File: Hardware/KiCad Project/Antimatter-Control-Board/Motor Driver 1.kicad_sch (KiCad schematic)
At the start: 3 parts, among them J2 MOTOR 1, U3 DRV8837

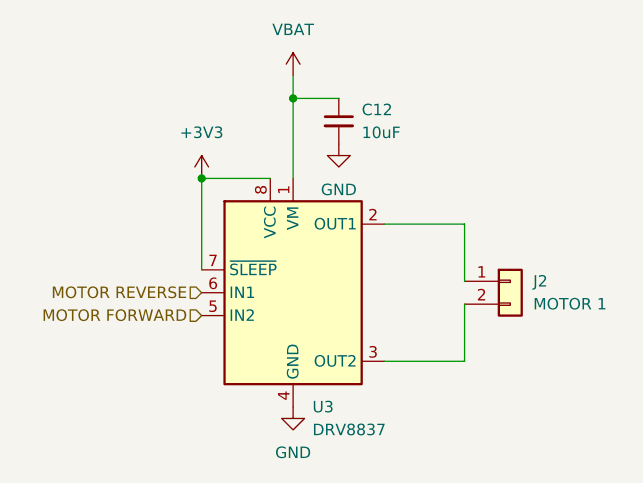
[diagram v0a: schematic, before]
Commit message: Update motor driver sheet
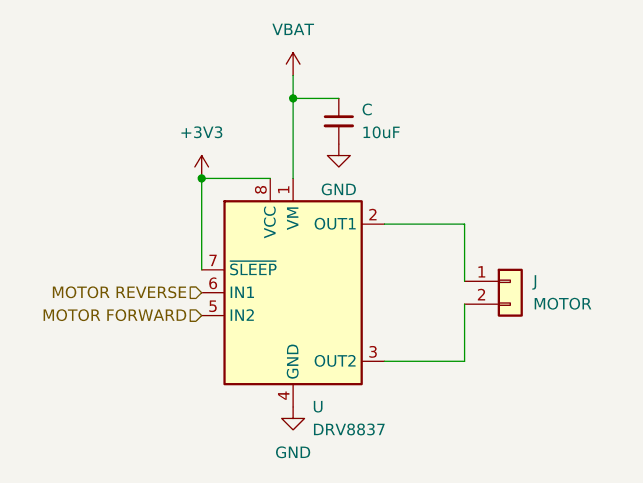
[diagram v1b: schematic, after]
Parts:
- J: renamed from J2; value MOTOR 1 -> MOTOR
- renumbered C12 to C, U3 to U
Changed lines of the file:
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@@
 		(dnp no)
 		(fields_autoplaced yes)
-		(property "Reference" "#PWR021"
+		(property "Reference" "#PWR"
 			(at 138.43 88.9 0)
 			(effects
@@
 		)
 		(instances
-			(project ""
-				(path "/ab2a7697-0e5e-4b53-bb59-6796636b3acd/d7ef5df8-638b-454c-90c6-da1c11f20dab"
-					(reference "#PWR021")
+			(project "Antimatter-Control-Board"
+				(path "/ab2a7697-0e5e-4b53-bb59-6796636b3acd/bd9e3a9b-0f0e-4e44-a772-4934aac148f4"
+					(reference "#PWR01")
 					(unit 1)
 				)
@@
 		(dnp no)
 		(fields_autoplaced yes)
-		(property "Reference" "#PWR020"
+		(property "Reference" "#PWR"
 			(at 148.59 116.84 0)
 			(effects
@@
 		)
 		(instances
-			(project ""
-				(path "/ab2a7697-0e5e-4b53-bb59-6796636b3acd/d7ef5df8-638b-454c-90c6-da1c11f20dab"
-					(reference "#PWR020")
+			(project "Antimatter-Control-Board"
+				(path "/ab2a7697-0e5e-4b53-bb59-6796636b3acd/bd9e3a9b-0f0e-4e44-a772-4934aac148f4"
+					(reference "#PWR028")
 					(unit 1)
 				)
@@
 		(instances
 			(project "Antimatter-Control-Board"
+				(path "/ab2a7697-0e5e-4b53-bb59-6796636b3acd/bd9e3a9b-0f0e-4e44-a772-4934aac148f4"
+					(reference "#PWR027")
+					(unit 1)
+				)
 				(path "/ab2a7697-0e5e-4b53-bb59-6796636b3acd/d7ef5df8-638b-454c-90c6-da1c11f20dab"
 					(reference "#PWR022")
@@
 		(dnp no)
 		(fields_autoplaced yes)
-		(property "Reference" "J2"
+		(property "Reference" "J"
 			(at 175.26 96.5199 0)
 			(effects
@@
 			)
 		)
-		(property "Value" "MOTOR 1"
+		(property "Value" "MOTOR"
 			(at 175.26 99.0599 0)
 			(effects
@@
 		)
 		(instances
-			(project ""
-				(path "/ab2a7697-0e5e-4b53-bb59-6796636b3acd/d7ef5df8-638b-454c-90c6-da1c11f20dab"
-					(reference "J2")
+			(project "Antimatter-Control-Board"
+				(path "/ab2a7697-0e5e-4b53-bb59-6796636b3acd/bd9e3a9b-0f0e-4e44-a772-4934aac148f4"
+					(reference "J3")
 					(unit 1)
 				)
@@
 		(dnp no)
 		(fields_autoplaced yes)
-		(property "Reference" "C12"
+		(property "Reference" "C"
 			(at 156.21 77.4762 0)
 			(effects
@@
 		)
 		(instances
-			(project ""
-				(path "/ab2a7697-0e5e-4b53-bb59-6796636b3acd/d7ef5df8-638b-454c-90c6-da1c11f20dab"
-					(reference "C12")
+			(project "Antimatter-Control-Board"
+				(path "/ab2a7697-0e5e-4b53-bb59-6796636b3acd/bd9e3a9b-0f0e-4e44-a772-4934aac148f4"
+					(reference "C7")
 					(unit 1)
 				)
@@
 		(dnp no)
 		(fields_autoplaced yes)
-		(property "Reference" "#PWR023"
+		(property "Reference" "#PWR"
 			(at 153.67 87.63 0)
 			(effects
@@
 		)
 		(instances
-			(project ""
-				(path "/ab2a7697-0e5e-4b53-bb59-6796636b3acd/d7ef5df8-638b-454c-90c6-da1c11f20dab"
-					(reference "#PWR023")
+			(project "Antimatter-Control-Board"
+				(path "/ab2a7697-0e5e-4b53-bb59-6796636b3acd/bd9e3a9b-0f0e-4e44-a772-4934aac148f4"
+					(reference "#PWR029")
 					(unit 1)
 				)
@@
 		(dnp no)
 		(fields_autoplaced yes)
-		(property "Reference" "U3"
+		(property "Reference" "U"
 			(at 150.7333 110.49 0)
 			(effects
@@
 		)
 		(instances
-			(project ""
-				(path "/ab2a7697-0e5e-4b53-bb59-6796636b3acd/d7ef5df8-638b-454c-90c6-da1c11f20dab"
-					(reference "U3")
-					(unit 1)
-				)
+			(project "Antimatter-Control-Board"
+				(path "/ab2a7697-0e5e-4b53-bb59-6796636b3acd/bd9e3a9b-0f0e-4e44-a772-4934aac148f4"
+					(reference "U1")
+					(unit 1)
+				)

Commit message: Change from nRF25832 to nRF25833 and copy reference schematic from datasheet
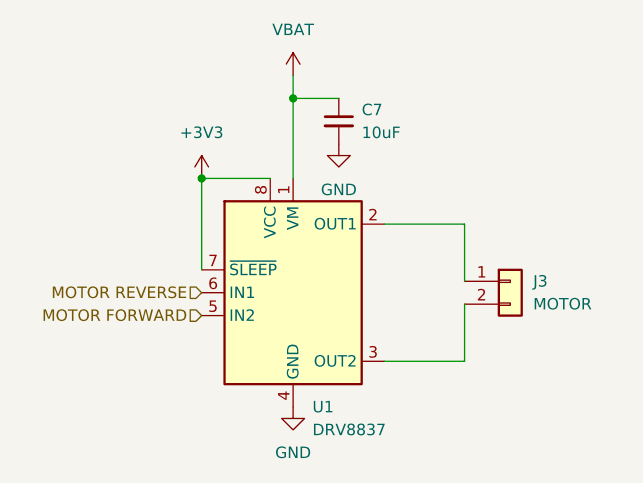
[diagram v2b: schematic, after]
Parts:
- renumbered C to C7, J to J3, U to U1
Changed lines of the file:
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@@
 		(dnp no)
 		(fields_autoplaced yes)
-		(property "Reference" "#PWR"
+		(property "Reference" "#PWR?"
 			(at 138.43 88.9 0)
 			(effects
@@
 					(unit 1)
 				)
+				(path "/ab2a7697-0e5e-4b53-bb59-6796636b3acd/d7ef5df8-638b-454c-90c6-da1c11f20dab"
+					(reference "#PWR?")
+					(unit 1)
+				)
 			)
 		)
@@
 		(dnp no)
 		(fields_autoplaced yes)
-		(property "Reference" "#PWR"
+		(property "Reference" "#PWR?"
 			(at 148.59 116.84 0)
 			(effects
@@
 					(unit 1)
 				)
+				(path "/ab2a7697-0e5e-4b53-bb59-6796636b3acd/d7ef5df8-638b-454c-90c6-da1c11f20dab"
+					(reference "#PWR?")
+					(unit 1)
+				)
 			)
 		)
@@
 		(dnp no)
 		(fields_autoplaced yes)
-		(property "Reference" "J"
+		(property "Reference" "J?"
 			(at 175.26 96.5199 0)
 			(effects
@@
 					(unit 1)
 				)
+				(path "/ab2a7697-0e5e-4b53-bb59-6796636b3acd/d7ef5df8-638b-454c-90c6-da1c11f20dab"
+					(reference "J?")
+					(unit 1)
+				)
 			)
 		)
@@
 		(dnp no)
 		(fields_autoplaced yes)
-		(property "Reference" "C"
+		(property "Reference" "C?"
 			(at 156.21 77.4762 0)
 			(effects
@@
 					(unit 1)
 				)
+				(path "/ab2a7697-0e5e-4b53-bb59-6796636b3acd/d7ef5df8-638b-454c-90c6-da1c11f20dab"
+					(reference "C?")
+					(unit 1)
+				)
 			)
 		)
@@
 		(dnp no)
 		(fields_autoplaced yes)
-		(property "Reference" "#PWR"
+		(property "Reference" "#PWR?"
 			(at 153.67 87.63 0)
 			(effects
@@
 					(unit 1)
 				)
+				(path "/ab2a7697-0e5e-4b53-bb59-6796636b3acd/d7ef5df8-638b-454c-90c6-da1c11f20dab"
+					(reference "#PWR?")
+					(unit 1)
+				)
 			)
 		)
@@
 		(dnp no)
 		(fields_autoplaced yes)
-		(property "Reference" "U"
+		(property "Reference" "U?"
 			(at 150.7333 110.49 0)
 			(effects
@@
 					(unit 1)
 				)
+				(path "/ab2a7697-0e5e-4b53-bb59-6796636b3acd/d7ef5df8-638b-454c-90c6-da1c11f20dab"
+					(reference "U?")
+					(unit 1)
+				)
